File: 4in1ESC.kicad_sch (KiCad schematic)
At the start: 62 parts, among them J1 SM08B-SRSS-TB, U1 INA199A1DCKR, U18 LMR51420YDDCR, U26 TPS746-3.3DRV, U5 XRIM160808SR47MBCD

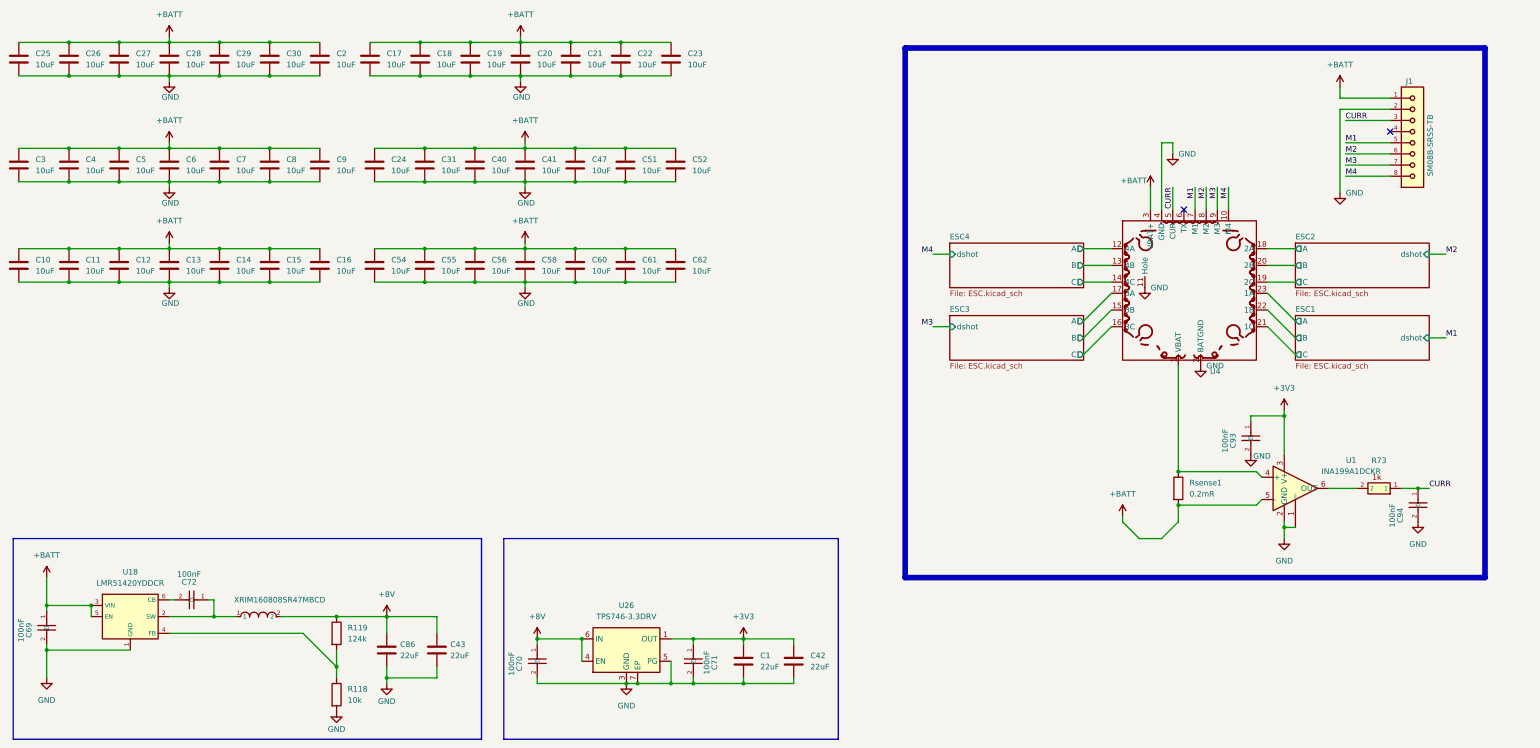
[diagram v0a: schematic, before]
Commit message: v0.4 component swap: INA186, TLV76733, JST symbol, ferrite bead
- Replace INA199A1DCKR with INA186A3IDCKR (C2058245) current sense amp
- Replace TPS746 with TLV76733DRVR (C2848334) LDO, SNS pin wired to output
- Add SM08B-SRSS-TB and INA186A3IDCKR symbols to local library
- Add JST 3D model (CONN-SMD_SR1.00-WS-8P.step) to footprint
- Add SC-70-6 3D model for INA186
- Update ferrite bead to BLM03PX121SN1D (C525479) in ESC sub-sheet
- Schematic ready for routing, DRC errors remain to fix

Co-Authored-By: Claude Opus 4.6 <noreply@anthropic.com>
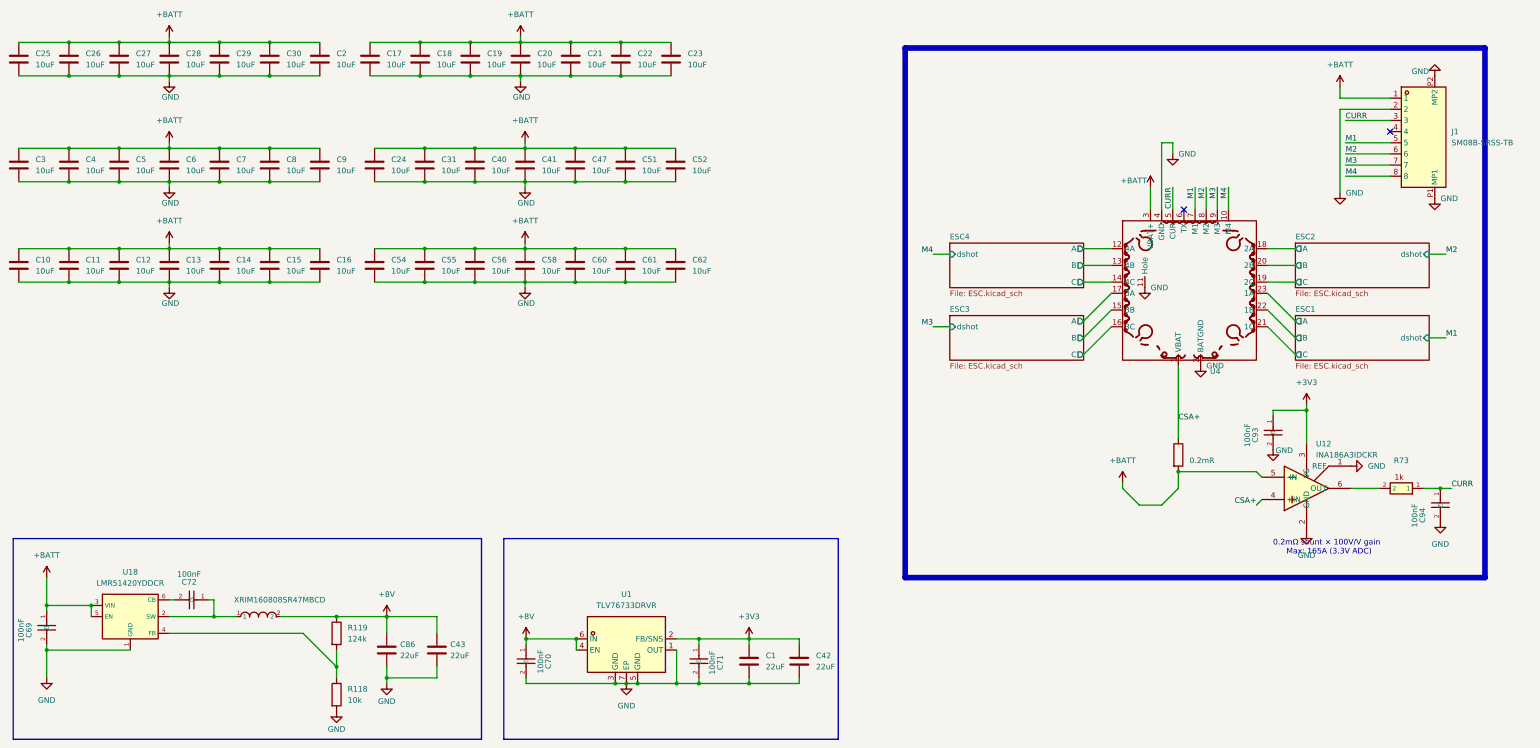
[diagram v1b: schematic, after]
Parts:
- removed J1: SM08B-SRSS-TB, Connector_JST:JST_SH_SM08B-SRSS-TB_1x08-1MP_P1.00mm_Horizontal, symbol SM08B-SRSS-TB:SM08B-SRSS-TB
- removed U1: INA199A1DCKR, Package_TO_SOT_SMD:SOT-363_SC-70-6, symbol Amplifier_Current:INA199xxDCK
- removed U26: TPS746-3.3DRV, Package_SON:WSON-6-1EP_2x2mm_P0.65mm_EP1x1.6mm, symbol Regulator_Linear:LP5912-3.3DRV
- added J1: SM08B-SRSS-TB, 4in1ESC:JST_SM08B-SRSS-TB, symbol components:SM08B-SRSS-TB
- added U1: TLV76733DRVR, 4in1ESC:WSON-6_L2.0-W2.0-P0.65-TL-EP, symbol components:TLV76733DRVR
- added U12: INA186A3IDCKR, 4in1ESC:SOT-363_SC-70-6, symbol components:INA186A3IDCKR
- U18: LCSC C5383002 -> C7296200
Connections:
- net +3V3: now also U1.2 (FB/SNS), U12.3 (VS)
- net +8V: now also U1.4 (EN), U1.6 (IN)
- net +BATT: now also J1.1, U12.5 (-IN)
- net CURR: now also J1.3
- net GND: now also J1.2, J1.P1 (MP1), J1.P2 (MP2), U1.1 (OUT), U1.3 (GND), U1.5 (GND), U1.7 (EP), U12.1 (REF), U12.2 (GND)
- net M1: now also J1.5
- net M2: now also J1.6
- net M3: now also J1.7
- net M4: now also J1.8
- net at R73.2: now also U12.6 (OUT)
- net CSA+: now reaches Rsense1.1, U4.1 (VBAT)
- net CSA+: now also U12.4 (+IN)
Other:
- note added: "0.2mΩ shunt × 100V/V gain Max: 165A (3.3V ADC)"
- moved on the sheet: C1, C42, C70, C71, C93, C94, R73
